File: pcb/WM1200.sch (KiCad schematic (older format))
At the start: 0 parts

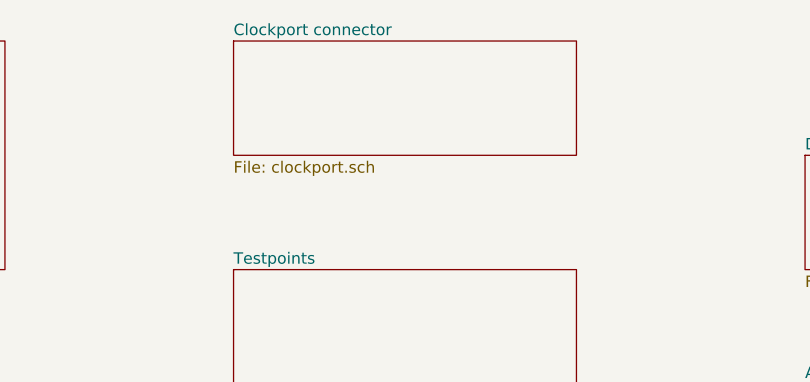
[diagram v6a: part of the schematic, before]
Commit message: clockport removed from ES1 pcb design (maybe another time)
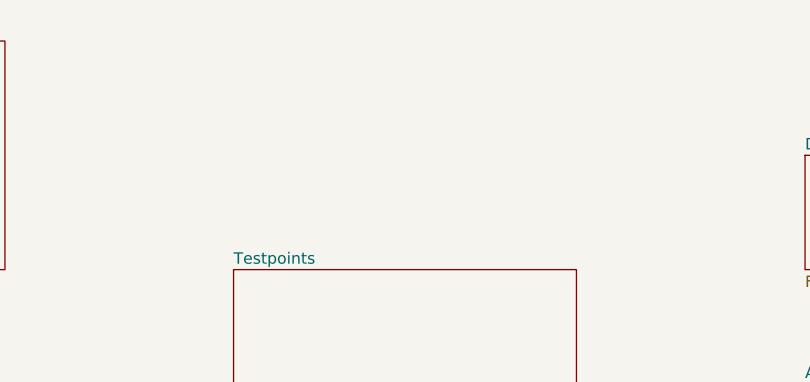
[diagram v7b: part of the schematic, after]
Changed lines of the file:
@@
-$EndSheet
-$Sheet
-S 3500 1000 1500 500
-U 5E55E8C3
-F0 "Clockport connector" 50
-F1 "clockport.sch" 50
 $EndSheet
 $Sheet
